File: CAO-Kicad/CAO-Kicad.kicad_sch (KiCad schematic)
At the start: 0 parts

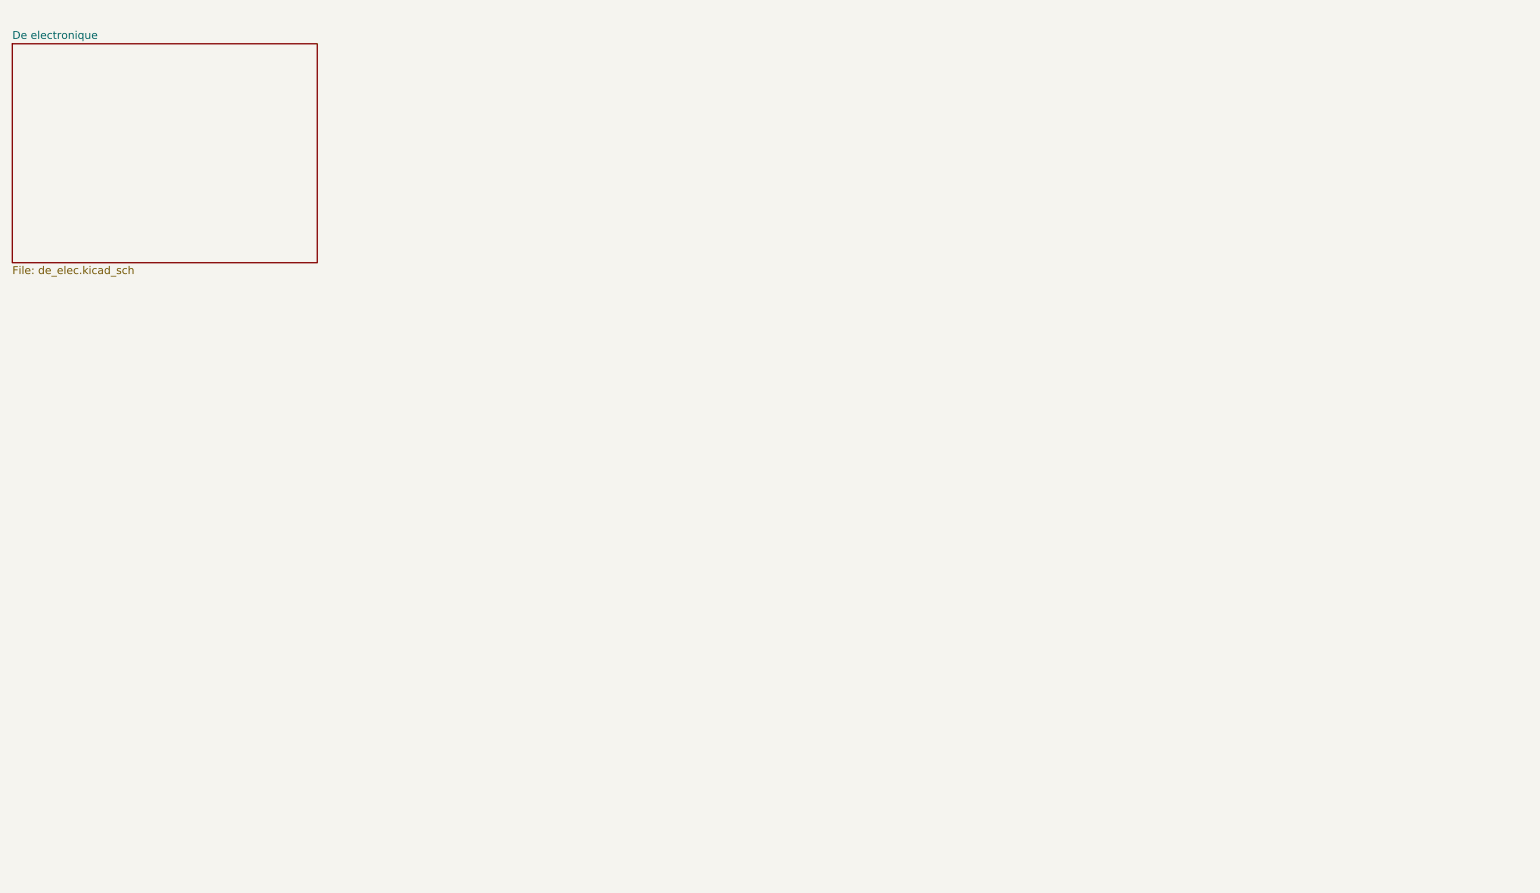
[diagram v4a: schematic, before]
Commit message: MAJ pour la realiser un PCB de 40x40 mm
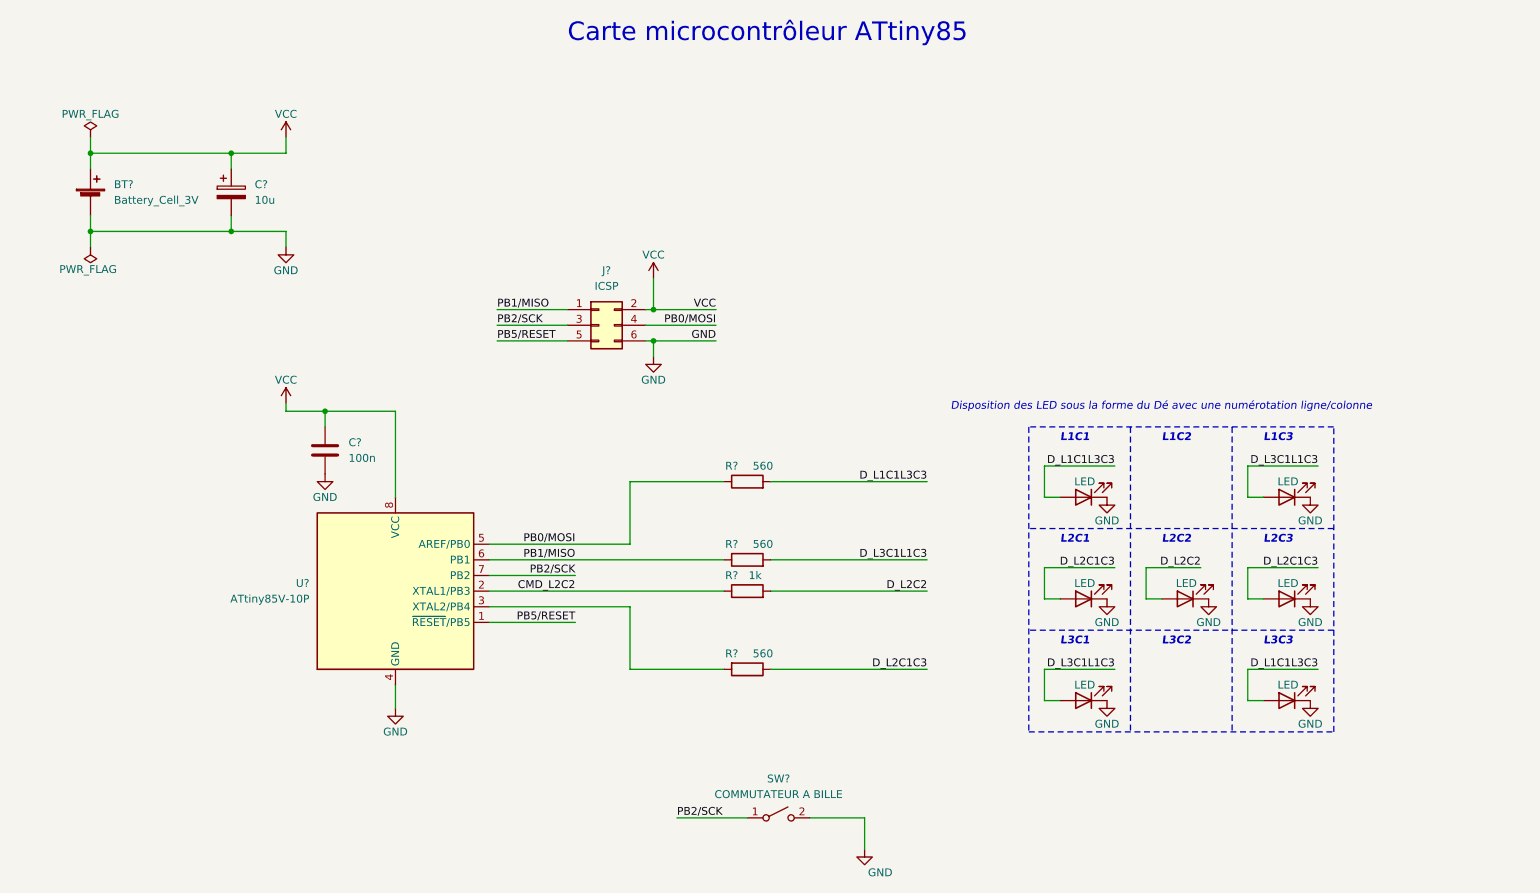
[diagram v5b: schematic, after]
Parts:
- added BT?: Battery_Cell_3V, Connector_PinHeader_2.54mm:PinHeader_1x02_P2.54mm_Vertical, symbol Device:Battery_Cell
- added C?: 100n, Capacitor_THT:C_Rect_L7.2mm_W3.0mm_P5.00mm_FKS2_FKP2_MKS2_MKP2, symbol Device:C
- added C?: 10u, Capacitor_THT:CP_Radial_D5.0mm_P2.50mm, symbol Device:C_Polarized
- added D_L1C? (x2), D_L2C? (x3), D_L3C? (x2): LED, LED_THT:LED_D5.0mm_Clear, symbol Device:LED
- added J?: ICSP, Connector_PinHeader_2.54mm:PinHeader_2x03_P2.54mm_Vertical, symbol Connector_Generic:Conn_02x03_Odd_Even
- added R? (x3): 560, Resistor_THT:R_Axial_DIN0207_L6.3mm_D2.5mm_P10.16mm_Horizontal, symbol Device:R
- added R?: 1k, Resistor_THT:R_Axial_DIN0207_L6.3mm_D2.5mm_P10.16mm_Horizontal, symbol Device:R
- added SW?: COMMUTATEUR A BILLE, Capacitor_THT:CP_Radial_D4.0mm_P2.00mm, symbol Switch:SW_SPST
- added U?: ATtiny85V-10P, Package_DIP:DIP-8_W7.62mm_LongPads, symbol MCU_Microchip_ATtiny:ATtiny85V-10P
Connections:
- new net: R?.2, U?.3 (XTAL2/PB4)
- new net CMD_L2C2: R?.1, U?.2 (XTAL1/PB3)
- new net D_L1C1L3C3: D_L1C?.2 (A), D_L3C?.2 (A), R?.2
- new net D_L2C1C3: D_L2C?.2 (A), D_L2C?.2 (A), R?.1
- new net D_L2C2: D_L2C?.2 (A), R?.2
- new net D_L3C1L1C3: D_L1C?.2 (A), D_L3C?.2 (A), R?.2
- new net GND: BT?.2 (-), C?.2, C?.2, D_L1C?.1 (K), D_L1C?.1 (K), D_L2C?.1 (K), D_L2C?.1 (K), D_L2C?.1 (K), D_L3C?.1 (K), D_L3C?.1 (K), J?.6 (Pin_6), SW?.2 (B), U?.4 (GND)
- new net PB0/MOSI: J?.4 (Pin_4), R?.1, U?.5 (AREF/PB0)
- new net PB1/MISO: J?.1 (Pin_1), R?.1, U?.6 (PB1)
- new net PB2/SCK: J?.3 (Pin_3), SW?.1 (A), U?.7 (PB2)
- new net PB5/RESET: J?.5 (Pin_5), U?.1 (~{RESET}/PB5)
- new net VCC: BT?.1 (+), C?.1, C?.1, J?.2 (Pin_2), U?.8 (VCC)
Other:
- removed sheet De electronique
- note added: "Carte microcontrôleur ATtiny85"
- note added: "Disposition des LED sous la forme du Dé avec une numérotation ligne/colonne"
- note added: "L1C1"
- note added: "L1C2"
- note added: "L1C3"
- note added: "L2C1"
- note added: "L2C2"
- note added: "L2C3"
- note added: "L3C1"
- note added: "L3C2"
- note added: "L3C3"

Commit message: Routage de la carte electronique
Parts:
- gave numbers to parts that had none: 17

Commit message: MAJ nommenclature
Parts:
- removed D_L1C3, D_L2C1, D_L2C2, D_L2C3, D_L3C1, D_L3C3: LED, LED_THT:LED_D5.0mm_Clear, symbol Device:LED
- added D2, D3, D4, D5, D6, D7: LED, LED_THT:LED_D5.0mm_Clear, symbol Device:LED
- renumbered D_L1C1 to D1, BT1 to J1, J1 to J2
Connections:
- net D_L2C2: now also D4.2 (A)
- net GND: now also D2.1 (K), D3.1 (K), D4.1 (K), D5.1 (K), D6.1 (K), D7.1 (K)
- net CMD_L2C1_L2C3: now reaches R4.2, U1.3 (XTAL2/PB4)
- net D_L1C1L3C3 renamed D_L1C1_L3C3
- net D_L1C1_L3C3: now also D7.2 (A)
- net D_L2C1C3 renamed D_L2C1_L2C3
- net D_L2C1_L2C3: now also D2.2 (A), D6.2 (A)
- net D_L3C1L1C3 renamed D_L3C1_L1C3
- net D_L3C1_L1C3: now also D3.2 (A), D5.2 (A)
- net PB0/MOSI renamed MOSI
- net PB1/MISO renamed MISO
- net PB2/SCK renamed SCK
- net PB5/RESET renamed ~{RESET}
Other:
- note added: "Programmation ISP : PB0/MOSI PB1/MISO PB2/SCK PB5/RESET"
- company: (none) -> FabTronic
- title: De-electronique -> Dé électronique
- moved on the sheet: J2, R1, R2, R3, R4, SW1
